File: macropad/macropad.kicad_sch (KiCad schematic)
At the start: 41 parts, among them J1 Conn_ARM_JTAG_SWD_10, J2 USB_C_Receptacle_USB2.0_16P, J3 Conn_01x03_Socket, U1 nPM1300-QEXX, U2 nRF52840, Y1 32MHz, Y2 32.768kHz

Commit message: finished macropad schematic
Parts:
- added 22pF: C, symbol Device:C
- added C27, C31, C33, C34, C39: 1uF, symbol Device:C
- added C28, C35: 100nF, symbol Device:C
- added C29: 47uF, symbol Device:C
- added C30, C36, C37, C38: 22uF, symbol Device:C
- added C32: 22pF, symbol Device:C
- added D1, D10, D11, D12, D14, D2, D3, D4, D5, D6, D7, D8, D9: 1N4148WS, symbol Device:D
- added D13: ESD2CAN24DBZRQ1, symbol Device:D_TVS_Dual_AAC
- added J4: Screen_Socket, symbol Connector:Conn_01x05_Socket
- added J5: Conn_Left, symbol Connector:Conn_01x05_Pin
- added J6: Conn_Right, symbol Connector:Conn_01x05_Pin
- added J7: Conn_Bottom, symbol Connector:Conn_01x05_Pin
- added L5: 1uH, symbol Device:L
- added R4: 511k, symbol Device:R
- added R5: 91k, symbol Device:R
- added R6: 100k, symbol Device:R
- added R7, R8: 120, symbol Device:R
- added SW1, SW10, SW11, SW12, SW2, SW3, SW4, SW5, SW6, SW7, SW8, SW9: SW_Push, symbol Switch:SW_Push
- added SW13: SW_Mode, symbol Switch:SW_SPDT
- added SW14: SW_Ship, symbol Switch:SW_Push
- added SW15: SW_Reset, symbol Switch:SW_Push
- added SW16: RotaryEncoder_Switch, symbol Device:RotaryEncoder_Switch
- added U3: USBLC6-2SC6, Package_TO_SOT_SMD:SOT-23-6, symbol Power_Protection:USBLC6-2SC6
- added U4: TPS631000, Package_TO_SOT_SMD:SOT-583-8, symbol meow:TPS631000
- added U5: TCAN337, symbol Interface_CAN_LIN:TCAN337
- added U6: MCP2515-xML, Package_DFN_QFN:QFN-20-1EP_4x4mm_P0.5mm_EP2.7x2.7mm, symbol meow:MCP2515-xML
- added Y3: 16Mhz, symbol Device:Crystal_GND23
- J1: value Conn_ARM_JTAG_SWD_10 -> JTAG_SWD
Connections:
- net +3V3_MCU: now also J4.3 (Pin_3)
- net GND: now also 22pF.1, C27.1, C28.1, C29.2, C30.1, C31.1, C32.1, C33.2, C34.1, C35.1, C36.2, C37.2, C38.2, C39.1, D13.3 (common), J4.4 (Pin_4), J5.2 (Pin_2), J5.4 (Pin_4), J6.2 (Pin_2), J6.4 (Pin_4), J7.2 (Pin_2), J7.4 (Pin_4), R5.2, R6.2, SW13.2 (B), SW14.1, SW15.1, SW16.C, U3.2 (GND), U4.6 (MODE), U4.7 (GND), U5.2 (GND), U5.8 (S), U6.8 (VSS), Y3.2 (G), Y3.3 (G)
- net PWR_SCL: now also U2.AC19 (P0.23)
- net PWR_SDA: now also U2.AD20 (P0.24)
- net PWR_SHPHLD: now also SW14.2
- net PWR_VSYS: now also C30.2, U4.4 (VIN)
- net USB_D+: now also U2.AD6 (D+), U3.1 (I/O1); no longer J2.A6 (D+), J2.B6 (D+)
- net USB_D-: now also U2.AD4 (D-), U3.3 (I/O2); no longer J2.A7 (D-), J2.B7 (D-)
- net VBUS_IN: now reaches J2.A4 (VBUS), J2.A9 (VBUS), J2.B4 (VBUS), J2.B9 (VBUS), U1.21 (VBUS)
- net VBUS_IN: now also C27.2
- net VBUS: now reaches C14.2, U2.AD2 (VBUS)
- net VBUS: now also U1.22 (VBUSOUT), C39.2, U3.5 (VBUS)
- net BLUETOOTH_~{EN}: now reaches U2.AC11 (P0.16)
- net BLUETOOTH_~{EN}: now also SW13.1 (A)
- net EC_B: now reaches U2.AC15 (P0.19)
- net EC_B: now also SW16.B
- net CAN_INT: now reaches U2.AC17 (P0.21)
- net CAN_INT: now also U6.11 (~{INT})
- net CAN_SPI_CS: now reaches U2.AC21 (P0.25)
- net CAN_SPI_CS: now also U6.16 (~{CS})
- net KEY_ROW_3: now reaches U2.AC9 (P0.14)
- net KEY_ROW_3: now also D10.1 (K), D11.1 (K), D12.1 (K), D9.1 (K)
- net EXT_BUCK_EN: now reaches U2.AD10 (P0.15)
- net EXT_BUCK_EN: now also R6.1, U4.5 (EN)
- net EC_A: now reaches U2.AD12 (P0.17)
- net EC_A: now also SW16.A
- net CAN_RESET: now reaches U2.AD16 (P0.20)
- net CAN_RESET: now also U6.17 (~{RESET})
- net CAN_FAULT: now reaches U2.AD18 (P0.22)
- net CAN_FAULT: now also U5.5 (FAULT)
- net KEY_ROW_2: now reaches U2.AD8 (P0.13)
- net KEY_ROW_2: now also D5.1 (K), D6.1 (K), D7.1 (K), D8.1 (K)
- net SPI_MOSI: now reaches U2.J1 (AIN2/P0.04)
- net SPI_MOSI: now also J4.1 (Pin_1), U6.14 (SI)
- net KEY_COL_3: now reaches U2.J24 (NFC2/P0.10)
- net KEY_COL_3: now also SW11.2, SW3.2, SW7.2
- net SPI_CLK: now reaches U2.K2 (AIN3/P0.05)
- net SPI_CLK: now also J4.2 (Pin_2), U6.12 (SCK)
- net SPI_MISO: now reaches U2.L1 (P0.06)
- net SPI_MISO: now also U6.15 (SO)
- net KEY_COL_2: now reaches U2.L24 (NFC1/P0.09)
- net KEY_COL_2: now also SW10.2, SW2.2, SW6.2
- net SCREEN_SPI_CS: now reaches U2.M2 (TRACECLK/P0.07)
- net SCREEN_SPI_CS: now also J4.5 (Pin_5)
- net KEY_COL_1: now reaches U2.N1 (P0.08)
- net KEY_COL_1: now also SW1.2, SW16.S2, SW5.2, SW9.2
- net KEY_COL_4: now reaches U2.T2 (TRACEDATA2/P0.11)
- net KEY_COL_4: now also SW12.2, SW4.2, SW8.2
- net KEY_ROW_1: now reaches U2.U1 (TRACEDATA1/P0.12)
- net KEY_ROW_1: now also D1.1 (K), D14.1 (K), D2.1 (K), D3.1 (K), D4.1 (K)
- net RESET renamed MCU_RESET
- net MCU_RESET: now also SW15.2
- new net: D10.2 (A), SW10.1
- new net: D1.2 (A), SW1.1
- new net: D11.2 (A), SW11.1
- new net: D7.2 (A), SW7.1
- new net: R4.2, R5.1, U4.8 (FB)
- new net: D3.2 (A), SW3.1
- new net: D6.2 (A), SW6.1
- new net: D9.2 (A), SW9.1
- new net: C33.1, R7.2, R8.1
- new net: L5.1, U4.2 (LX2)
- new net: L5.2, U4.3 (LX1)
- new net: C32.2, U6.6 (OSC2), Y3.1
- new net: 22pF.2, U6.7 (OSC1), Y3.4
- new net: D2.2 (A), SW2.1
- new net: D8.2 (A), SW8.1
- new net: D5.2 (A), SW5.1
- new net: D14.2 (A), SW16.S1
- new net: D12.2 (A), SW12.1
- new net: D4.2 (A), SW4.1
- new net +EXT_3V3: C28.2, C29.1, C31.2, C34.2, C35.2, C36.1, C37.1, C38.1, J5.3 (Pin_3), J6.3 (Pin_3), J7.3 (Pin_3), R4.1, U4.1 (VOUT), U5.3 (VCC), U6.18 (VDD)
- new net CAN_H: D13.1 (A1), J5.1 (Pin_1), J6.1 (Pin_1), J7.1 (Pin_1), R7.1, U5.7 (CANH)
- new net CAN_L: D13.2 (A2), J5.5 (Pin_5), J6.5 (Pin_5), J7.5 (Pin_5), R8.2, U5.6 (CANL)
- new net CAN_RX: U5.4 (RXD), U6.20 (RXCAN)
- new net CAN_TX: U5.1 (TXD), U6.19 (TXCAN)
- new net RAW_USB_D+: J2.A6 (D+), J2.B6 (D+), U3.6 (I/O1)
- new net RAW_USB_D-: J2.A7 (D-), J2.B7 (D-), U3.4 (I/O2)
- no-connect marks 14 -> 39
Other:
- moved on the sheet: AE1, C1, C10, C11, C12, C13, C14, C15, C16, C17, C18, C19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

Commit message: schematic cleanup
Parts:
- removed 22pF: C, symbol Device:C
- added C40: 22pF, symbol Device:C
- added D15: BLUE, symbol Device:LED
- added D16: RED, symbol Device:LED
- added R9: 1k, symbol Device:R
- added TP1: +BATT, symbol Connector:TestPoint
- added TP2: +VSYS, symbol Connector:TestPoint
- added TP3: VBUS, symbol Connector:TestPoint
- added TP4: +EXT_3V3, symbol Connector:TestPoint
- added TP5: +3V3_MCU, symbol Connector:TestPoint
- added TP6: GND, symbol Connector:TestPoint
- J3: value Conn_01x03_Socket -> Batt_Socket
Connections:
- net +BATT: now also TP1.1
- net +EXT_3V3: now also TP4.1
- net GND: now also U6.21 (EP), C40.1, D15.1 (K), TP6.1
- net PWR_INT: now also U2.H2 (P0.27)
- net PWR_VSYS: now also D16.2 (A), TP2.1
- net USB_CC1: now reaches J2.A5 (CC1), U1.23 (CC1)
- net USB_CC2: now reaches J2.B5 (CC2), U1.24 (CC2)
- net at U6.7 (OSC1), Y3.4: now also C40.2
- net at U2.G1 (P0.26): now also R9.2
- net at U1.26 (LED1): now also D16.1 (K)
- net +3V3_MCU renamed +MCU_3V3
- net +MCU_3V3: now also TP5.1
- net VBUS_IN renamed +VBUS_IN
- net +VBUS_IN: now also TP3.1
- new net: D15.2 (A), R9.1
- no-connect marks 39 -> 42
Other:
- note added: "Buttons"
- note added: "CanBus"
- note added: "Connectors"
- note added: "I am Receptacle"
- note added: "MCU"
- note added: "MCU JTAG"
- note added: "Power"
- note added: "stuff"
- moved on the sheet: AE1, C1, C10, C11, C12, C13, C14, C15, C16, C17, C18, C19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

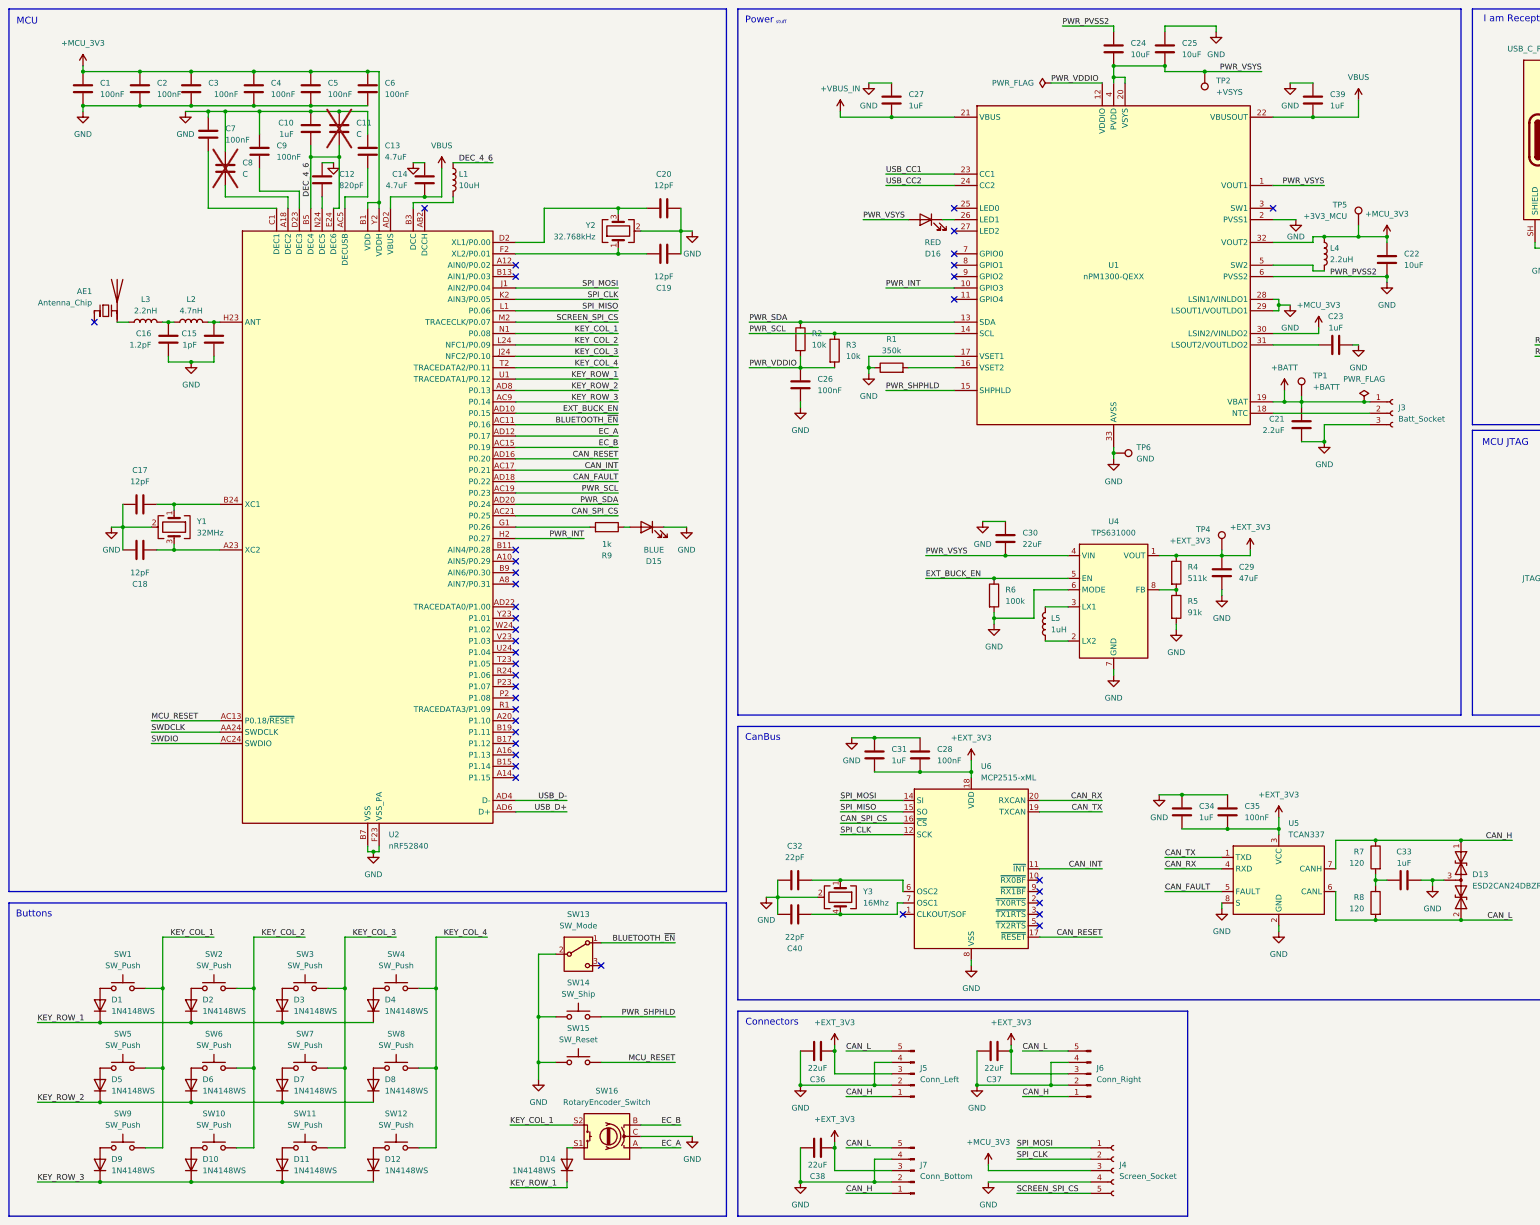
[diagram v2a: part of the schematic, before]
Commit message: journal+pcb: lcsc ids, mpns, 3d models of components
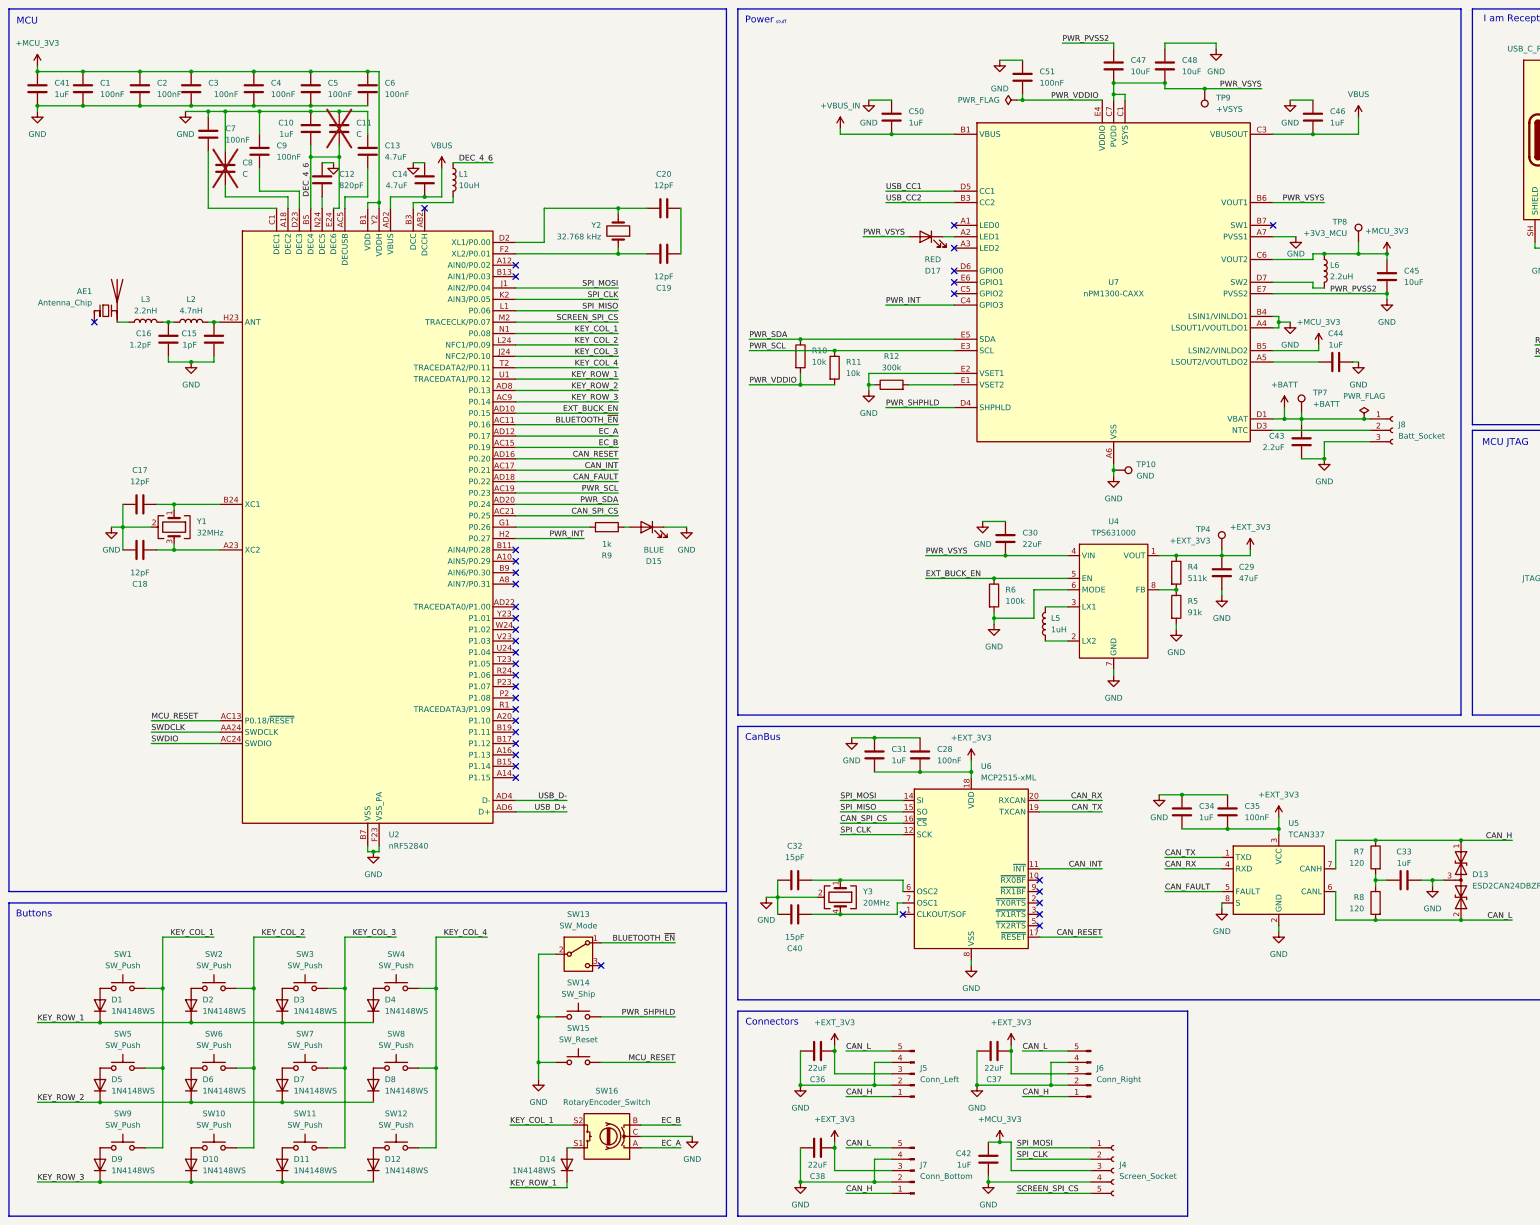
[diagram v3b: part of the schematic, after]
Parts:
- removed C21: 2.2uF, symbol Device:C
- removed C22, C24, C25: 10uF, symbol Device:C
- removed C23, C27, C39: 1uF, symbol Device:C
- removed C26: 100nF, symbol Device:C
- removed D16: RED, symbol Device:LED
- removed J3: Batt_Socket, symbol Connector:Conn_01x03_Socket
- removed L4: 2.2uH, symbol Device:L
- removed R1: 350k, symbol Device:R
- removed R2, R3: 10k, symbol Device:R
- removed TP1: +BATT, symbol Connector:TestPoint
- removed TP2: +VSYS, symbol Connector:TestPoint
- removed TP5: +3V3_MCU, symbol Connector:TestPoint
- removed TP6: GND, symbol Connector:TestPoint
- removed U1: nPM1300-QEXX, Package_DFN_QFN:QFN-32-1EP_5x5mm_P0.5mm_EP3.6x3.6mm_ThermalVias, symbol PCM_nordic-lib-kicad-npm:nPM1300-QEXX
- removed Y2: 32.768kHz, symbol Device:Crystal_GND24
- added C41, C42, C44, C46, C50: 1uF, Capacitor_SMD:C_0603_1608Metric, symbol Device:C
- added C43: 2.2uF, Capacitor_SMD:C_0603_1608Metric, symbol Device:C
- added C45, C47, C48: 10uF, Capacitor_SMD:C_0603_1608Metric, symbol Device:C
- added C51: 100nF, Capacitor_SMD:C_0603_1608Metric, symbol Device:C
- added D17: RED, LED_SMD:LED_0603_1608Metric, symbol Device:LED
- added J8: Batt_Socket, Connector_PinHeader_2.00mm:PinHeader_1x05_P2.00mm_Vertical, symbol Connector:Conn_01x03_Socket
- added L6: 2.2uH, Inductor_SMD:L_0805_2012Metric, symbol Device:L
- added R10, R11: 10k, Resistor_SMD:R_0603_1608Metric, symbol Device:R
- added R12: 300k, Resistor_SMD:R_0603_1608Metric, symbol Device:R
- added TP10: GND, TestPoint:TestPoint_Pad_D1.5mm, symbol Connector:TestPoint
- added TP7: +BATT, TestPoint:TestPoint_Pad_D1.5mm, symbol Connector:TestPoint
- added TP8: +3V3_MCU, TestPoint:TestPoint_Pad_D1.5mm, symbol Connector:TestPoint
- added TP9: +VSYS, TestPoint:TestPoint_Pad_D1.5mm, symbol Connector:TestPoint
- added U7: nPM1300-CAXX, PCM_nordic-lib-kicad-npm:BGA-35_7x5_3.077x2.3775mm, symbol PCM_nordic-lib-kicad-npm:nPM1300-CAXX
- added Y2: 32.768 kHz, Crystal:Crystal_SMD_2012-2Pin_2.0x1.2mm, symbol Device:Crystal
- AE1: footprint (none) -> Diode_SMD:D_1206_3216Metric; LCSC (none) -> C293767; MPN (none) -> ANT3216LL00R2400A
- C1, C2, C28, C3, C35, C4, C5, C6, C7, C9: footprint (none) -> Capacitor_SMD:C_0603_1608Metric; LCSC (none) -> C14663; MPN (none) -> CC0603KRX7R9BB104
- C10, C31, C33, C34: footprint (none) -> Capacitor_SMD:C_0603_1608Metric; LCSC (none) -> C5199872; MPN (none) -> CL10B105KB8NQNC
- C12: footprint (none) -> Capacitor_SMD:C_0603_1608Metric; LCSC (none) -> C107057; MPN (none) -> CC0603JRNPO9BN821
- C13, C14: footprint (none) -> Capacitor_SMD:C_0603_1608Metric; LCSC (none) -> C389010; MPN (none) -> GRM188Z71C475KE21D
- C15: footprint (none) -> Capacitor_SMD:C_0402_1005Metric; LCSC (none) -> C309455; MPN (none) -> CC0402BRNPO9BN1R0
- C16: footprint (none) -> Capacitor_SMD:C_0402_1005Metric; LCSC (none) -> C327292; MPN (none) -> CC0402BRNPO9BN1R2
- C17, C18, C19, C20: footprint (none) -> Capacitor_SMD:C_0603_1608Metric; LCSC (none) -> C519450; MPN (none) -> CC0603GRNPO9BN120
- C29: footprint (none) -> Capacitor_SMD:C_0805_2012Metric; LCSC (none) -> C124129; MPN (none) -> GRM21BR61A476ME15L
- C30, C36, C37, C38: footprint (none) -> Capacitor_SMD:C_0805_2012Metric; LCSC (none) -> C29277; MPN (none) -> CL21A226MPQNNNE
- C32, C40: value 22pF -> 15pF; footprint (none) -> Capacitor_SMD:C_0603_1608Metric; LCSC (none) -> C519451; MPN (none) -> CC0603GRNPO9BN150
- D1, D10, D11, D12, D14, D2, D3, D4, D5, D6, D7, D8, D9: footprint (none) -> Diode_SMD:D_SOD-323; LCSC (none) -> C917117; MPN (none) -> 1N4148WS
- D13: footprint (none) -> Package_TO_SOT_SMD:SOT-23-3; MPN (none) -> ESD2CAN24DBZRQ1
- D15: footprint (none) -> LED_SMD:LED_0603_1608Metric; LCSC (none) -> C51933294; MPN (none) -> GL0603UB01
- J1: footprint (none) -> Connector_PinHeader_1.27mm:PinHeader_2x05_P1.27mm_Vertical
- J2: footprint (none) -> Connector_USB:USB_C_Receptacle_G-Switch_GT-USB-7010ASV; LCSC (none) -> C2988369; MPN (none) -> GT-USB-7010ASV
- J4, J5, J6, J7: footprint (none) -> Connector_PinHeader_2.00mm:PinHeader_1x05_P2.00mm_Vertical
- L1: footprint (none) -> Inductor_SMD:L_0603_1608Metric; LCSC (none) -> C194437; MPN (none) -> MLZ1608N100LT000
- L2: footprint (none) -> Inductor_SMD:L_0402_1005Metric; LCSC (none) -> C86065; MPN (none) -> LQG15HS4N7S02D
- L3: footprint (none) -> Inductor_SMD:L_0402_1005Metric; LCSC (none) -> C86061; MPN (none) -> LQG15HS2N2S02D
- L5: footprint (none) -> Inductor_SMD:L_1008_2520Metric; LCSC (none) -> C882955; MPN (none) -> DFE252012P-1R0M=P2
- R4: footprint (none) -> Resistor_SMD:R_0603_1608Metric; LCSC (none) -> C2930114; MPN (none) -> FRC0603F5113TS
- R5: footprint (none) -> Resistor_SMD:R_0603_1608Metric; LCSC (none) -> C2907077; MPN (none) -> FRC0603F9102TS
- R6: footprint (none) -> Resistor_SMD:R_0603_1608Metric; LCSC (none) -> C2906980; MPN (none) -> FRC0603F1003TS
- R7, R8: footprint (none) -> Resistor_SMD:R_0603_1608Metric; LCSC (none) -> C2906988; MPN (none) -> FRC0603F1200TS
- R9: footprint (none) -> Resistor_SMD:R_0603_1608Metric; LCSC (none) -> C2907002; MPN (none) -> FRC0603F1001TS
- SW1, SW10, SW11, SW12, SW2, SW3, SW4, SW5, SW6, SW7, SW8, SW9: footprint (none) -> PCM_Switch_Keyboard_Hotswap_Kailh:SW_Hotswap_Kailh_Choc_V1V2_1.00u
- SW13: footprint (none) -> meow:SW-SMD_MK-12C02-G020; LCSC (none) -> C963206; MPN (none) -> MK-12C02-G020
- SW14: footprint (none) -> meow:KEY-SMD_SKRTLAE010; LCSC (none) -> C110293; MPN (none) -> SKRTLAE010
- SW15: footprint (none) -> meow:KEY-SMD_B3U-1000PM; LCSC (none) -> C231329; MPN (none) -> B3U-1000P
- SW16: footprint (none) -> Rotary_Encoder:RotaryEncoder_Alps_EC11E-Switch_Vertical_H20mm; LCSC (none) -> C470742; MPN (none) -> EC11E09244BS
- TP3, TP4: footprint (none) -> TestPoint:TestPoint_Pad_D1.5mm
- U2: MPN (none) -> NRF52840-QIAA-F-R7
- U3: LCSC (none) -> C2827654; MPN (none) -> USBLC6-2SC6
- U4: LCSC (none) -> C5219190; MPN (none) -> TPS631000DRLR
- U5: footprint (none) -> Package_SO:SOIC-8_3.9x4.9mm_P1.27mm; LCSC (none) -> C2860648; MPN (none) -> TCAN337DR
- U6: LCSC (none) -> C96140; MPN (none) -> MCP2515T-I/ML
- Y1: footprint (none) -> Crystal:Crystal_SMD_2016-4Pin_2.0x1.6mm; LCSC (none) -> C5339095; MPN (none) -> TX201632M4BBCE2T
- Y3: value 16Mhz -> 20MHz; footprint (none) -> Crystal:Crystal_SMD_3225-4Pin_3.2x2.5mm; LCSC (none) -> C42420972; MPN (none) -> 2.1.3.1600011
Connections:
- net +BATT: now also C43.1, J8.1 (Pin_1), TP7.1, U7.D1 (VBAT), U7.D2 (VBAT)
- net +MCU_3V3: now also C41.1, C42.1, C45.1, L6.1, TP8.1, U7.B5 (LSIN2/VINLDO2), U7.C6 (VOUT2)
- net +VBUS_IN: now also C50.2, U7.B1 (VBUS), U7.B2 (VBUS)
- net GND: now also C41.2, C42.2, C43.2, C44.2, C45.2, C46.1, C47.1, C48.1, C50.1, C51.1, J8.3 (Pin_3), R12.1, TP10.1, U7.A4 (LSOUT1/VOUTLDO1), U7.A6 (VSS), U7.A7 (PVSS1), U7.B4 (LSIN1/VINLDO1), U7.E2 (VSET1), U7.E7 (PVSS2); no longer C19.2, C20.2
- net PWR_INT: now also U7.C4 (GPIO3)
- net PWR_SCL: now also R11.1, U7.E3 (SCL)
- net PWR_SDA: now also R10.1, U7.E5 (SDA)
- net PWR_SHPHLD: now also U7.D4 (SHPHLD)
- net PWR_VDDIO: now also C51.2, R10.2, R11.2, U7.E4 (VDDIO)
- net PWR_VSYS: now also C47.2, C48.2, D17.2 (A), TP9.1, U7.B6 (VOUT1), U7.C1 (VSYS), U7.C2 (VSYS), U7.C7 (PVDD)
- net USB_CC1: now also U7.D5 (CC1)
- net USB_CC2: now also U7.B3 (CC2)
- net VBUS: now also C46.2, U7.C3 (VBUSOUT)
- net at C19.1, U2.F2 (XL2/P0.01): now also Y2.1
- net at C20.1, U2.D2 (XL1/P0.00): now also Y2.2
- new net: C19.2, C20.2
- new net: D17.1 (K), U7.A2 (LED1)
- new net: C44.1, U7.A5 (LSOUT2/VOUTLDO2)
- new net: J8.2 (Pin_2), U7.D3 (NTC)
- new net: L6.2, U7.D7 (SW2)
- new net: R12.2, U7.E1 (VSET2)
- no-connect marks 42 -> 41
